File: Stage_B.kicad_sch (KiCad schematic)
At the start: 0 parts

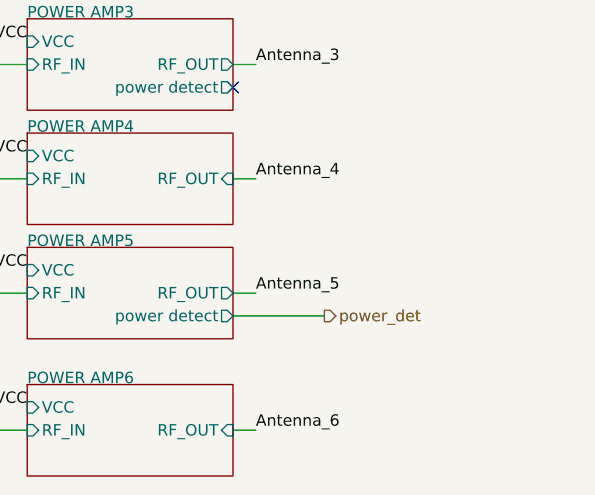
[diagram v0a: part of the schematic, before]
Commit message: created fab files, needs some cleanup
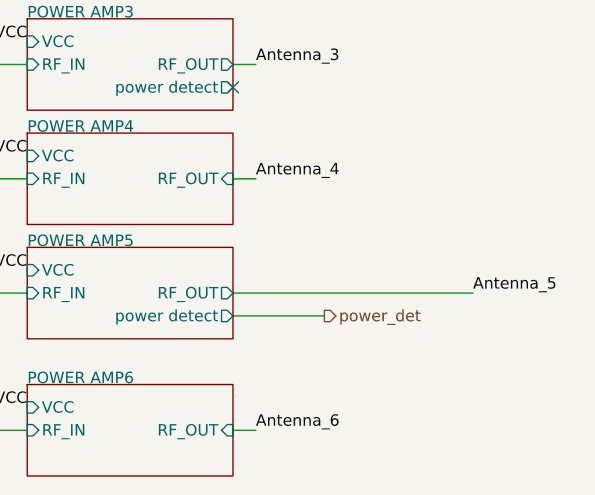
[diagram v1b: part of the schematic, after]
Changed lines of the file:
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@@
 	(wire
 		(pts
-			(xy 210.82 91.44) (xy 208.28 91.44)
+			(xy 234.95 91.44) (xy 208.28 91.44)
 		)
 		(stroke
@@
 	)
 	(label "Antenna_5"
-		(at 210.82 91.44 0)
+		(at 234.95 91.44 0)
 		(effects
 			(font
@@
 		)
 	)
+	(netclass_flag ""
+		(length 2.54)
+		(shape round)
+		(at 209.55 40.64 180)
+		(fields_autoplaced yes)
+		(effects
+			(font
+				(size 1.27 1.27)
+			)
+			(justify right bottom)
+		)
+		(property "Net Class" "50ohm_antenna_feed"
+			(at 210.2485 43.18 0)
+			(show_name no)
+			(do_not_autoplace no)
+			(effects
+				(font
+					(size 1.27 1.27)
+				)
+				(justify left)
+			)
+		)
+		(property "Component Class" ""
+			(at 208.28 -30.48 0)
+			(show_name no)
+			(do_not_autoplace no)
+			(effects
+				(font
+					(size 1.27 1.27)
+					(italic yes)
+				)
+			)
+		)
+	)
+	(netclass_flag ""
+		(length 2.54)
+		(shape round)
+		(at 233.68 91.44 180)
+		(fields_autoplaced yes)
+		(effects
+			(font
+				(size 1.27 1.27)
+			)
+			(justify right bottom)
+		)
+		(property "Net Class" "50ohm_antenna_feed"
+			(at 234.3785 93.98 0)
+			(show_name no)
+			(do_not_autoplace no)
+			(effects
+				(font
+					(size 1.27 1.27)
+				)
+				(justify left)
+			)
+		)
+		(property "Component Class" ""
+			(at 232.41 20.32 0)
+			(show_name no)
+			(do_not_autoplace no)
+			(effects
+				(font
+					(size 1.27 1.27)
+					(italic yes)
+				)
+			)
+		)
+	)
+	(netclass_flag ""
+		(length 2.54)
+		(shape round)
+		(at 209.55 106.68 180)
+		(fields_autoplaced yes)
+		(effects
+			(font
+				(size 1.27 1.27)
+			)
+			(justify right bottom)
+		)
+		(property "Net Class" "50ohm_antenna_feed"
+			(at 210.2485 109.22 0)
+			(show_name no)
+			(do_not_autoplace no)
+			(effects
+				(font
+					(size 1.27 1.27)
+				)
+				(justify left)
+			)
+		)
+		(property "Component Class" ""
+			(at 208.28 35.56 0)
+			(show_name no)
+			(do_not_autoplace no)
+			(effects
+				(font
+					(size 1.27 1.27)
+					(italic yes)
+				)
+			)
+		)
+	)
+	(netclass_flag ""
+		(length 2.54)
+		(shape round)
+		(at 209.55 78.74 180)
+		(fields_autoplaced yes)
+		(effects
+			(font
+				(size 1.27 1.27)
+			)
+			(justify right bottom)
+		)
+		(property "Net Class" "50ohm_antenna_feed"
+			(at 210.2485 81.28 0)
+			(show_name no)
+			(do_not_autoplace no)
+			(effects
+				(font
+					(size 1.27 1.27)
+				)
+				(justify left)
+			)
+		)
+		(property "Component Class" ""
+			(at 208.28 7.62 0)
+			(show_name no)
+			(do_not_autoplace no)
+			(effects
+				(font
+					(size 1.27 1.27)
+					(italic yes)
+				)
+			)
+		)
+	)
+	(netclass_flag ""
+		(length 2.54)
+		(shape round)
+		(at 209.55 53.34 180)
+		(fields_autoplaced yes)
+		(effects
+			(font
+				(size 1.27 1.27)
+			)
+			(justify right bottom)
+		)
+		(property "Net Class" "50ohm_antenna_feed"
+			(at 210.2485 55.88 0)
+			(show_name no)
+			(do_not_autoplace no)
+			(effects
+				(font
+					(size 1.27 1.27)
+				)
+				(justify left)
+			)
+		)
+		(property "Component Class" ""
+			(at 208.28 -17.78 0)
+			(show_name no)
+			(do_not_autoplace no)
+			(effects
+				(font
+					(size 1.27 1.27)
+					(italic yes)
+				)
+			)
+		)
+	)
+	(netclass_flag ""
+		(length 2.54)
+		(shape round)
+		(at 209.55 66.04 180)
+		(fields_autoplaced yes)
+		(effects
+			(font
+				(size 1.27 1.27)
+			)
+			(justify right bottom)
+		)
+		(property "Net Class" "50ohm_antenna_feed"
+			(at 210.2485 68.58 0)
+			(show_name no)
+			(do_not_autoplace no)
+			(effects
+				(font
+					(size 1.27 1.27)
+				)
+				(justify left)
+			)
+		)
+		(property "Component Class" ""
+			(at 208.28 -5.08 0)
+			(show_name no)
+			(do_not_autoplace no)
+			(effects
+				(font
+					(size 1.27 1.27)
+					(italic yes)
+				)
+			)
+		)
+	)
